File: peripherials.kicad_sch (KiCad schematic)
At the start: 59 parts, among them U15 PN7160AHN

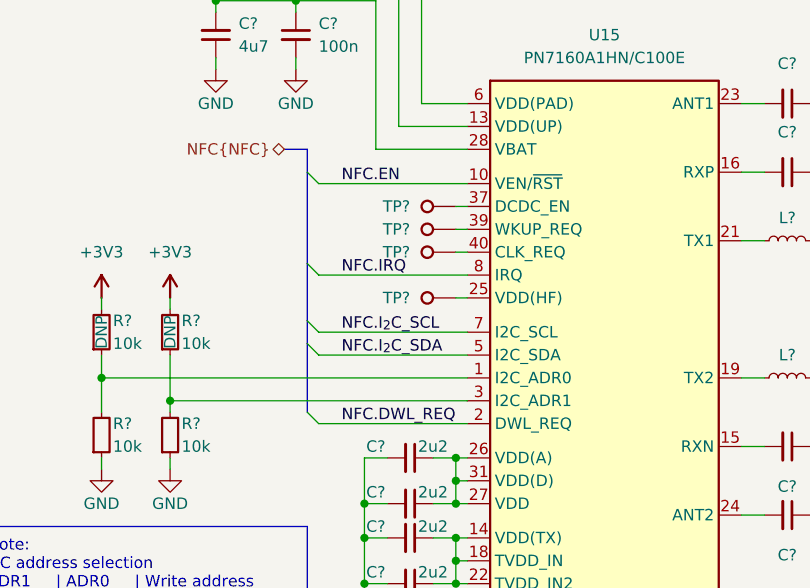
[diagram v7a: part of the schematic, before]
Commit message: [#54617] Connect VSYNC0/1 & WKUP_REQ through 0R-DNP to CM
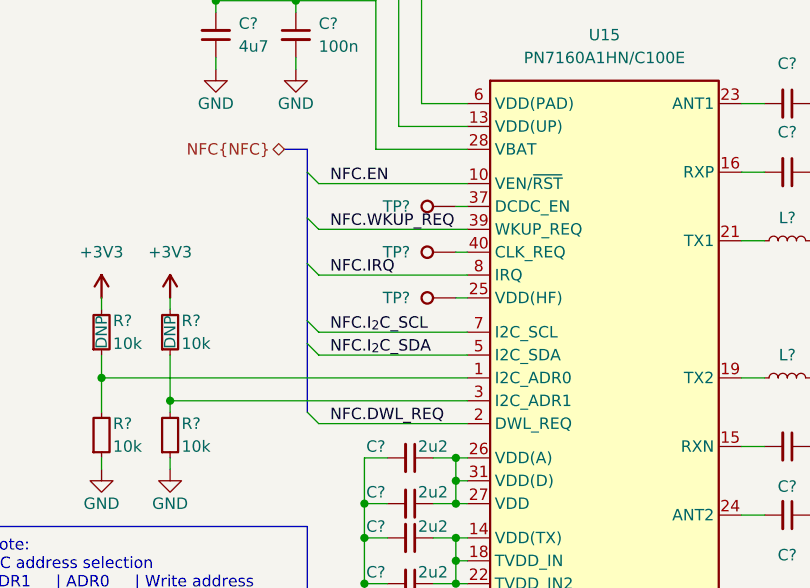
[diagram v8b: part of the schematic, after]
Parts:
- removed TP?: TP_1mm_SMD, antmicro-footprints:TP_SMD_1mm, symbol antmicroTestPoints:TP_1mm_SMD
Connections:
- net NFC.WKUP_REQ: now reaches U15.39 (WKUP_REQ)
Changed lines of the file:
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@@
     (comment 1 "www.antmicro.com")
   )
-  (bus_alias "NFC" (members "EN" "IRQ" "DWL_REQ" "I_{2}C_SDA" "I_{2}C_SCL"))
+  (bus_alias "NFC" (members "EN" "IRQ" "DWL_REQ" "I_{2}C_SDA" "I_{2}C_SCL" "WKUP_REQ"))
   (junction (at 248.92 55.88) (diameter 0) (color 0 0 0 0)
   )
@@
     (stroke (width 0) (type default) (color 0 0 0 0))
   )
+  (bus_entry (at 260.35 106.68) (size -1.27 -1.27)
+    (stroke (width 0) (type default) (color 0 0 0 0))
+  )
   (bus_entry (at 111.76 182.88) (size 2.54 2.54)
     (stroke (width 0) (type default) (color 0 0 0 0))
@@
     (stroke (width 0) (type default) (color 0 0 0 0))
   )
-  (wire (pts (xy 275.59 106.68) (xy 276.86 106.68))
+  (wire (pts (xy 132.08 210.82) (xy 114.3 210.82))
     (stroke (width 0) (type default) (color 0 0 0 0))
   )
-  (wire (pts (xy 132.08 210.82) (xy 114.3 210.82))
+  (bus (pts (xy 259.08 105.41) (xy 259.08 110.49))
     (stroke (width 0) (type default) (color 0 0 0 0))
   )
@@
     (stroke (width 0) (type default) (color 0 0 0 0))
   )
+  (wire (pts (xy 260.35 106.68) (xy 276.86 106.68))
+    (stroke (width 0) (type default) (color 0 0 0 0))
+  )
   (wire (pts (xy 350.52 115.57) (xy 350.52 116.84))
     (stroke (width 0) (type default) (color 0 0 0 0))
@@
     (stroke (width 0) (type default) (color 0 0 0 0))
   )
-  (bus (pts (xy 259.08 100.33) (xy 259.08 110.49))
+  (bus (pts (xy 259.08 100.33) (xy 259.08 105.41))
     (stroke (width 0) (type default) (color 0 0 0 0))
   )
@@
     (effects (font (size 1.27 1.27)) (justify right bottom))
   )
-  (label "NFC.DWL_REQ" (at 262.89 128.27 0)
+  (label "NFC.DWL_REQ" (at 261.62 128.27 0)
     (effects (font (size 1.27 1.27)) (justify left bottom))
   )
@@
     (effects (font (size 1.27 1.27)) (justify right bottom))
   )
-  (label "NFC.IRQ" (at 262.89 111.76 0)
+  (label "NFC.IRQ" (at 261.62 111.76 0)
     (effects (font (size 1.27 1.27)) (justify left bottom))
   )
@@
     (effects (font (size 1.27 1.27)) (justify right bottom))
   )
-  (label "NFC.I_{2}C_SCL" (at 262.89 118.11 0)
+  (label "NFC.I_{2}C_SCL" (at 261.62 118.11 0)
     (effects (font (size 1.27 1.27)) (justify left bottom))
   )
@@
     (effects (font (size 1.27 1.27)) (justify left bottom))
   )
+  (label "NFC.WKUP_REQ" (at 261.62 106.68 0)
+    (effects (font (size 1.27 1.27)) (justify left bottom))
+  )
   (label "GPIO.17" (at 128.27 185.42 180)
     (effects (font (size 1.27 1.27)) (justify right bottom))
@@
     (effects (font (size 1.27 1.27)) (justify right bottom))
   )
-  (label "NFC.I_{2}C_SDA" (at 262.89 120.65 0)
+  (label "NFC.I_{2}C_SDA" (at 261.62 120.65 0)
     (effects (font (size 1.27 1.27)) (justify left bottom))
   )
@@
     (effects (font (size 1.27 1.27)) (justify left bottom))
   )
-  (label "NFC.EN" (at 262.89 101.6 0)
+  (label "NFC.EN" (at 261.62 101.6 0)
     (effects (font (size 1.27 1.27)) (justify left bottom))
   )
@@
     (pin "2")
   )
-  (symbol (lib_id "antmicroTestPoints:TP_1mm_SMD") (at 275.59 106.68 180) (unit 1)
-    (in_bom yes) (on_board yes) (fields_autoplaced)
-    (property "Reference" "TP?" (id 0) (at 270.51 106.6799 0)
-      (effects (font (size 1.27 1.27) (thickness 0.15)) (justify left))
-    )
-    (property "Value" "TP_1mm_SMD" (id 1) (at 260.35 99.06 0)
-      (effects (font (size 1.27 1.27) (thickness 0.15)) (justify left bottom) hide)
-    )
-    (property "Footprint" "antmicro-footprints:TP_SMD_1mm" (id 2) (at 260.35 96.52 0)
-      (effects (font (size 1.27 1.27) (thickness 0.15)) (justify left bottom) hide)
-    )
-    (property "Datasheet" "" (id 3) (at 260.35 93.98 0)
-      (effects (font (size 1.27 1.27) (thickness 0.15)) (justify left bottom) hide)
-    )
-    (property "Author" "Antmicro" (id 4) (at 260.35 91.44 0)
-      (effects (font (size 1.27 1.27) (thickness 0.15)) (justify left bottom) hide)
-    )
-    (property "License" "Apache-2.0" (id 5) (at 260.35 88.9 0)
-      (effects (font (size 1.27 1.27) (thickness 0.15)) (justify left bottom) hide)
-    )
-    (property "MPN" "" (id 6) (at 275.59 106.68 0)
-      (effects (font (size 1.27 1.27)) hide)
-    )
-    (property "Manufacturer" "" (id 7) (at 275.59 106.68 0)
-      (effects (font (size 1.27 1.27)) hide)
-    )
-    (pin "1")
-  )
   (symbol (lib_id "antmicropower:+5V") (at 58.42 177.8 0) (unit 1)
